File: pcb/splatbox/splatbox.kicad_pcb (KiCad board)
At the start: 2 copper layers, 258.5 x 110 mm, 18 parts, among them SW1 Switch, SW10 Switch, SW11 Switch, SW12 Switch, SW13 Switch, SW14 Switch, SW15 Switch, SW2 Switch, SW3 Switch, SW4 Switch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

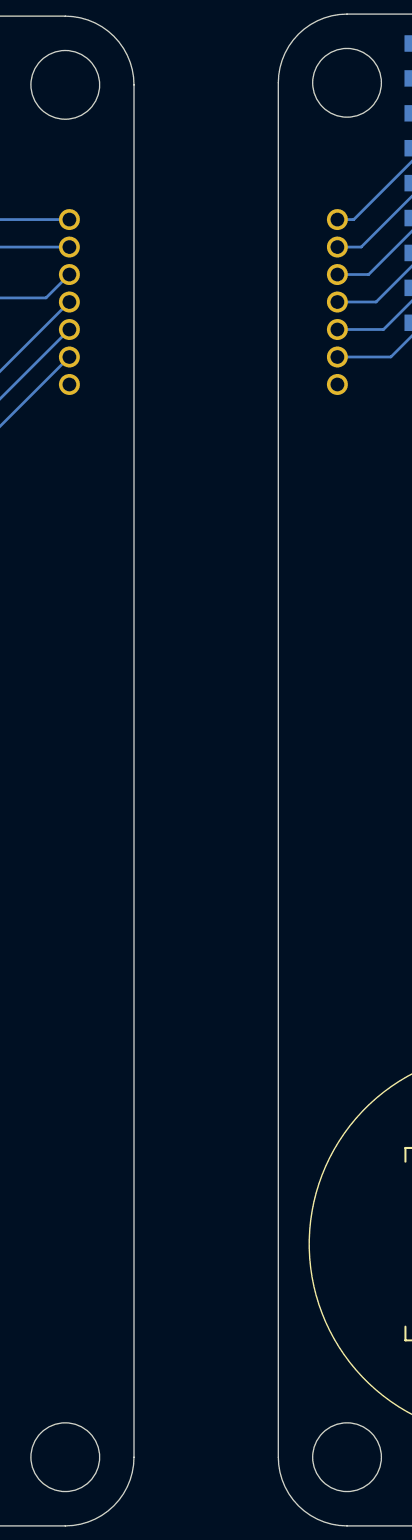
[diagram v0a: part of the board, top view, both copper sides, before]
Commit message: Add mousebites to connect panels; Add silk screen
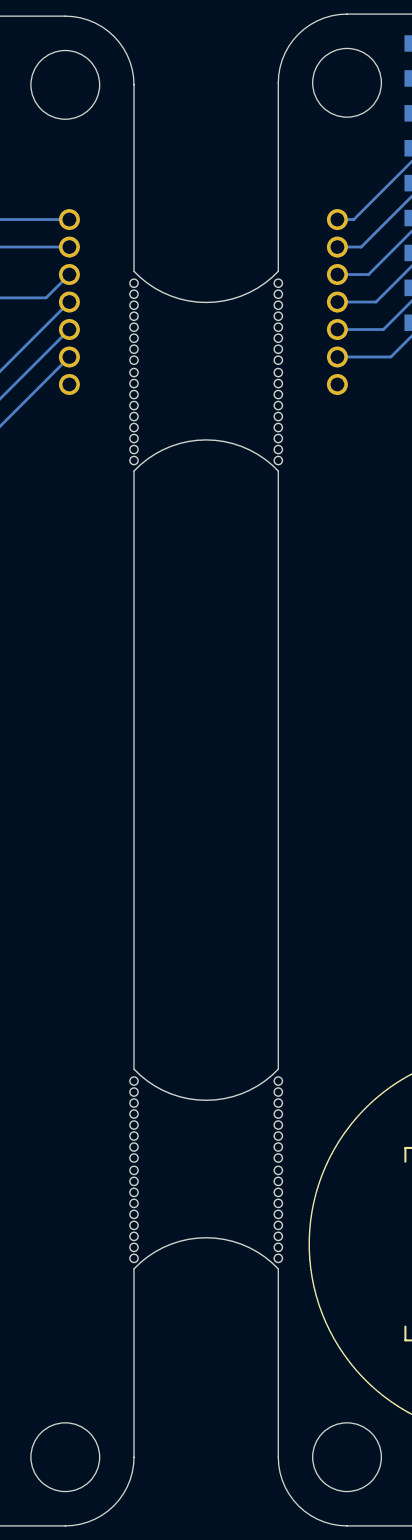
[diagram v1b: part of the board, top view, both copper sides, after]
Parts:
- added REF**: mousebites, CustomLibrary:mousebites, F.Cu at (164.5, 181.0)
- added REF**: mousebites, CustomLibrary:mousebites, F.Cu at (164.5, 123.0)
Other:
- outline, holes or cut-outs redrawn
